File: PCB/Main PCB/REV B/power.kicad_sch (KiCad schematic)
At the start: 14 parts, among them U5 AMS1117-3.3

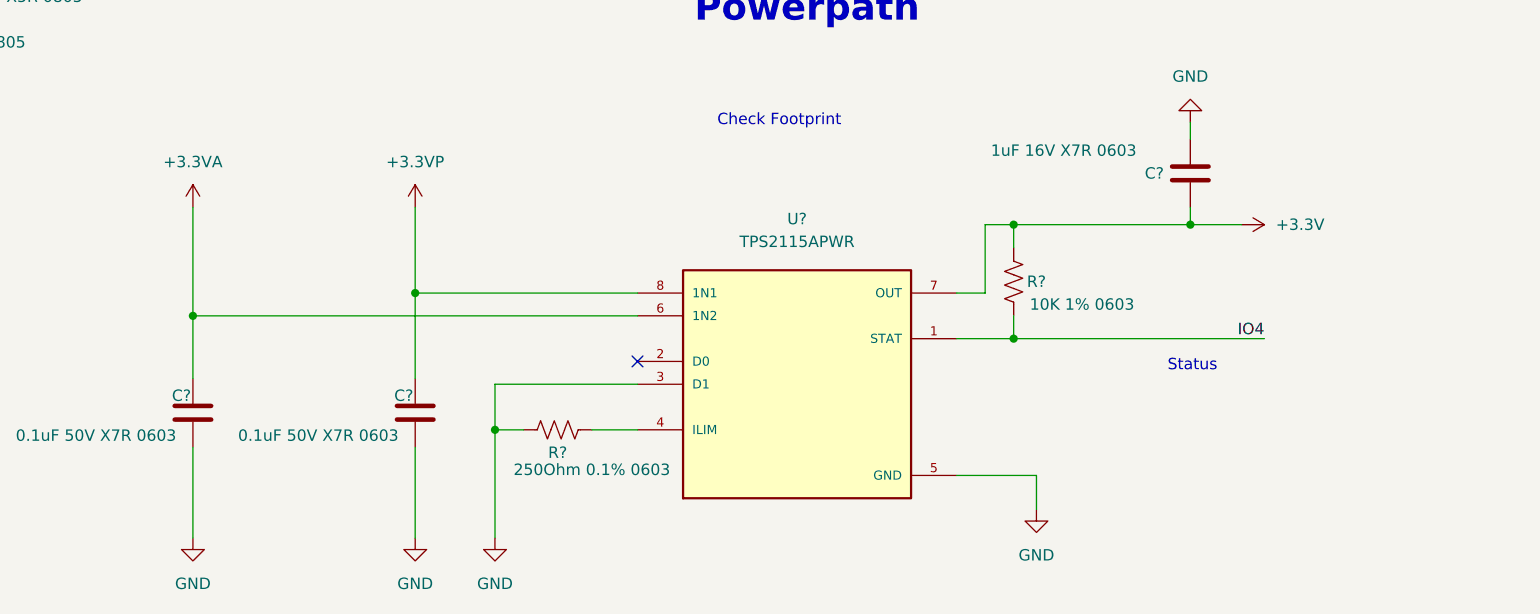
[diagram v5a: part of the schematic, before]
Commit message: Changed rotary encoder to incremental, nearly done design on rotary encoder
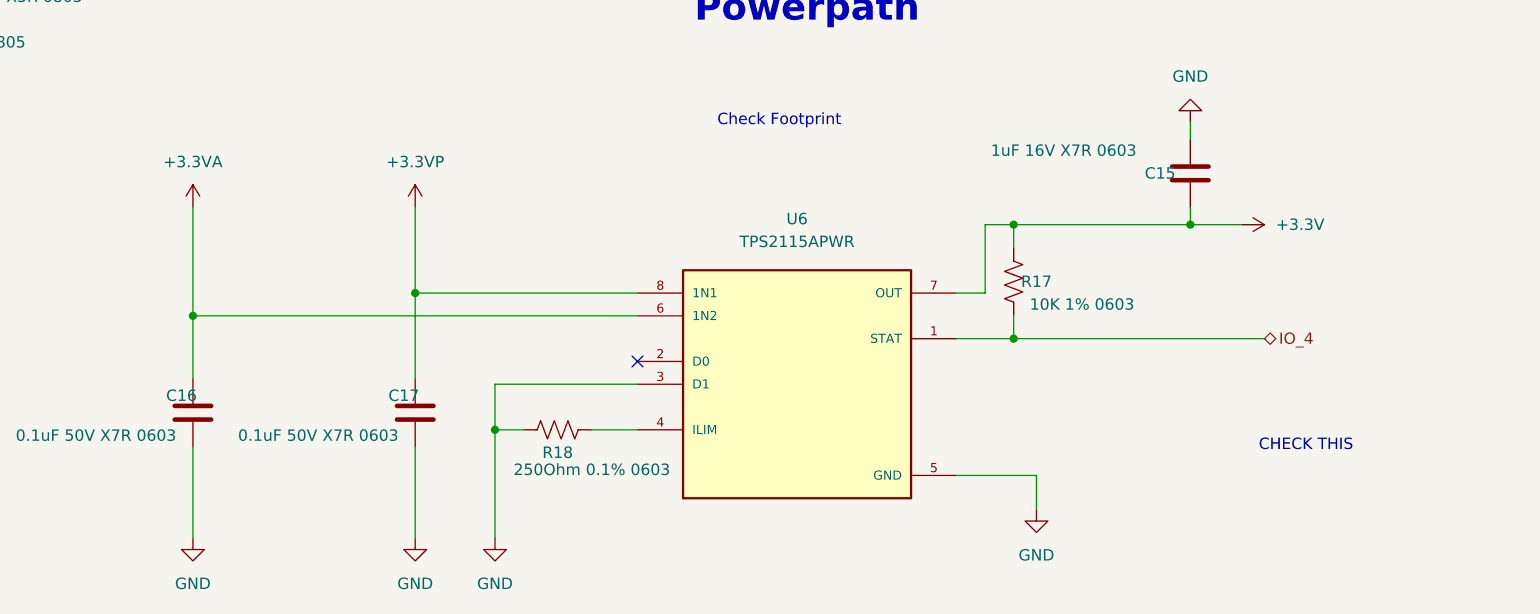
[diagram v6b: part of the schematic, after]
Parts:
- gave numbers to parts that had none: 6
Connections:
- net IO4 renamed IO_4
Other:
- note added: "CHECK THIS"
- note removed: "Status"
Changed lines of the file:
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@@
     (stroke (width 0) (type default) (color 0 0 0 0))
   )
-  (text "Status\n" (at 213.995 123.19 0)
+  (text "CHECK THIS\n" (at 224.155 132.08 0)
     (effects (font (size 1.27 1.27)) (justify left bottom))
   )
@@
     (effects (font (size 3 3) (thickness 1.016) bold) (justify left bottom))
   )
-  (label "IO4" (at 224.79 119.38 180)
-    (effects (font (size 1.27 1.27)) (justify right bottom))
-  )
   (hierarchical_label "AC_N" (shape input) (at 31.75 45.72 180)
     (effects (font (size 1.27 1.27)) (justify right))
@@
     (effects (font (size 1.27 1.27)) (justify right))
   )
+  (hierarchical_label "IO_4" (shape bidirectional) (at 224.79 119.38 0)
+    (effects (font (size 1.27 1.27)) (justify left))
+  )
   (symbol (lib_id "TPS2115APWR:TPS2115APWR") (at 172.72 124.46 0) (unit 1)
     (in_bom yes) (on_board yes) (fields_autoplaced)
-    (property "Reference" "U?" (id 0) (at 172.72 106.045 0))
+    (property "Reference" "U6" (id 0) (at 172.72 106.045 0))
     (property "Value" "TPS2115APWR" (id 1) (at 172.72 108.585 0))
     (property "Footprint" "Customs Smoker:SOP65P640X120-8N" (id 2) (at 172.72 124.46 0)
@@
   (symbol (lib_id "power:+3.3VP") (at 130.175 104.775 0) (unit 1)
     (in_bom yes) (on_board yes) (fields_autoplaced)
-    (property "Reference" "#PWR054" (id 0) (at 133.985 106.045 0)
+    (property "Reference" "#PWR056" (id 0) (at 133.985 106.045 0)
       (effects (font (size 1.27 1.27)) hide)
     )
@@
   (symbol (lib_id "power:GND") (at 105.41 141.605 0) (unit 1)
     (in_bom yes) (on_board yes) (fields_autoplaced)
-    (property "Reference" "#PWR?" (id 0) (at 105.41 147.955 0)
+    (property "Reference" "#PWR059" (id 0) (at 105.41 147.955 0)
       (effects (font (size 1.27 1.27)) hide)
     )
@@
   (symbol (lib_id "power:GND") (at 139.065 141.605 0) (unit 1)
     (in_bom yes) (on_board yes) (fields_autoplaced)
-    (property "Reference" "#PWR?" (id 0) (at 139.065 147.955 0)
+    (property "Reference" "#PWR061" (id 0) (at 139.065 147.955 0)
       (effects (font (size 1.27 1.27)) hide)
     )
@@
   (symbol (lib_id "Device:R_US") (at 146.05 129.54 270) (unit 1)
     (in_bom yes) (on_board yes)
-    (property "Reference" "R?" (id 0) (at 146.05 132.08 90))
+    (property "Reference" "R18" (id 0) (at 146.05 132.08 90))
     (property "Value" "250Ohm 0.1% 0603" (id 1) (at 149.86 133.985 90))
     (property "Footprint" "Resistor_SMD:R_0603_1608Metric" (id 2) (at 145.796 130.556 90)
@@
   (symbol (lib_id "Device:R_US") (at 196.85 113.03 0) (unit 1)
     (in_bom yes) (on_board yes)
-    (property "Reference" "R?" (id 0) (at 199.39 113.03 0))
+    (property "Reference" "R17" (id 0) (at 199.39 113.03 0))
     (property "Value" "10K 1% 0603" (id 1) (at 204.47 115.57 0))
     (property "Footprint" "Resistor_SMD:R_0603_1608Metric" (id 2) (at 197.866 113.284 90)
@@
   (symbol (lib_id "Device:C") (at 130.175 127.635 0) (mirror x) (unit 1)
     (in_bom yes) (on_board yes)
-    (property "Reference" "C?" (id 0) (at 128.905 125.73 0))
+    (property "Reference" "C17" (id 0) (at 128.905 125.73 0))
     (property "Value" "0.1uF 50V X7R 0603" (id 1) (at 119.38 130.175 0))
     (property "Footprint" "Capacitor_SMD:C_0603_1608Metric" (id 2) (at 131.1402 123.825 0)
@@
   (symbol (lib_id "power:+5V") (at 40.005 78.74 0) (unit 1)
     (in_bom yes) (on_board yes) (fields_autoplaced)
-    (property "Reference" "#PWR049" (id 0) (at 40.005 82.55 0)
+    (property "Reference" "#PWR051" (id 0) (at 40.005 82.55 0)
       (effects (font (size 1.27 1.27)) hide)
     )
@@
   (symbol (lib_id "power:+3.3V") (at 222.25 106.68 270) (unit 1)
     (in_bom yes) (on_board yes) (fields_autoplaced)
-    (property "Reference" "#PWR055" (id 0) (at 218.44 106.68 0)
+    (property "Reference" "#PWR057" (id 0) (at 218.44 106.68 0)
       (effects (font (size 1.27 1.27)) hide)
     )
@@
   (symbol (lib_id "power:+3.3V") (at 232.41 44.45 0) (mirror y) (unit 1)
     (in_bom yes) (on_board yes)
-    (property "Reference" "#PWR051" (id 0) (at 232.41 48.26 0)
+    (property "Reference" "#PWR048" (id 0) (at 232.41 48.26 0)
       (effects (font (size 1.27 1.27)) hide)
     )
@@
   (symbol (lib_id "power:+3.3VA") (at 105.41 104.775 0) (unit 1)
     (in_bom yes) (on_board yes) (fields_autoplaced)
-    (property "Reference" "#PWR058" (id 0) (at 105.41 108.585 0)
+    (property "Reference" "#PWR055" (id 0) (at 105.41 108.585 0)
       (effects (font (size 1.27 1.27)) hide)
     )
@@
   (symbol (lib_id "power:GND") (at 115.57 50.8 0) (unit 1)
     (in_bom yes) (on_board yes)
-    (property "Reference" "#PWR048" (id 0) (at 115.57 57.15 0)
+    (property "Reference" "#PWR050" (id 0) (at 115.57 57.15 0)
       (effects (font (size 1.27 1.27)) hide)
     )
@@
   (symbol (lib_id "Device:C") (at 105.41 127.635 0) (mirror x) (unit 1)
     (in_bom yes) (on_board yes)
-    (property "Reference" "C?" (id 0) (at 104.14 125.73 0))
+    (property "Reference" "C16" (id 0) (at 104.14 125.73 0))
     (property "Value" "0.1uF 50V X7R 0603" (id 1) (at 94.615 130.175 0))
     (property "Footprint" "Capacitor_SMD:C_0603_1608Metric" (id 2) (at 106.3752 123.825 0)
@@
   (symbol (lib_id "power:+3.3VP") (at 81.915 78.74 0) (unit 1)
     (in_bom yes) (on_board yes) (fields_autoplaced)
-    (property "Reference" "#PWR050" (id 0) (at 85.725 80.01 0)
+    (property "Reference" "#PWR052" (id 0) (at 85.725 80.01 0)
       (effects (font (size 1.27 1.27)) hide)
     )
@@
   (symbol (lib_id "power:GND") (at 216.535 95.25 180) (unit 1)
     (in_bom yes) (on_board yes) (fields_autoplaced)
-    (property "Reference" "#PWR?" (id 0) (at 216.535 88.9 0)
+    (property "Reference" "#PWR054" (id 0) (at 216.535 88.9 0)
       (effects (font (size 1.27 1.27)) hide)
     )
@@
   (symbol (lib_id "power:GND") (at 199.39 138.43 0) (unit 1)
     (in_bom yes) (on_board yes) (fields_autoplaced)
-    (property "Reference" "#PWR057" (id 0) (at 199.39 144.78 0)
+    (property "Reference" "#PWR058" (id 0) (at 199.39 144.78 0)
       (effects (font (size 1.27 1.27)) hide)
     )
@@
   (symbol (lib_id "power:GND") (at 130.175 141.605 0) (unit 1)
     (in_bom yes) (on_board yes) (fields_autoplaced)
-    (property "Reference" "#PWR?" (id 0) (at 130.175 147.955 0)
+    (property "Reference" "#PWR060" (id 0) (at 130.175 147.955 0)
       (effects (font (size 1.27 1.27)) hide)
     )
@@
   (symbol (lib_id "Device:C") (at 216.535 100.965 0) (unit 1)
     (in_bom yes) (on_board yes)
-    (property "Reference" "C?" (id 0) (at 211.455 100.965 0)
+    (property "Reference" "C15" (id 0) (at 211.455 100.965 0)
       (effects (font (size 1.27 1.27)) (justify left))
     )
@@
   (symbol (lib_id "power:+3.3V") (at 271.78 44.45 0) (mirror y) (unit 1)
     (in_bom yes) (on_board yes)
-    (property "Reference" "#PWR052" (id 0) (at 271.78 48.26 0)
-      (effects (font (size 1.27 1.27)) hide)
-    )
+    (property "Reference" "#PWR049" (id 0) (at 271.78 48.26 0)
+      (effects (font (size 1.27 1.27)) hide)
+    )
